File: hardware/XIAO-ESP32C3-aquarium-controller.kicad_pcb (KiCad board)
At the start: 2 copper layers, 70 x 100 mm, 43 parts, among them J1 Conn_01x02, J2 Conn_01x07, J3 Conn_01x06, J4 Conn_01x03, J5 Conn_01x03, K1 SANYOU_SRD_Form_C, K2 SANYOU_SRD_Form_C, K3 SANYOU_SRD_Form_C, Q1 AO3400A, Q2 AO3400A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

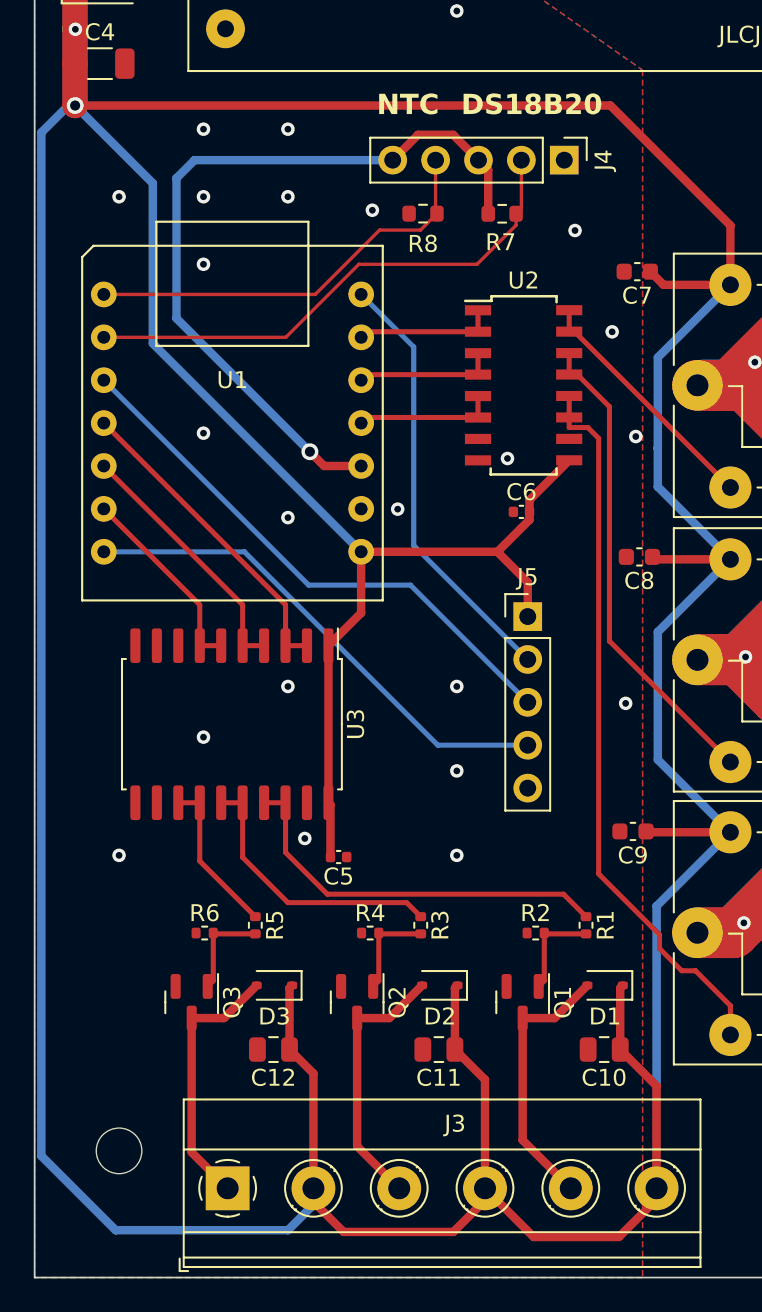
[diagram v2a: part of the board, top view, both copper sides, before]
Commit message: add + pad for 5V
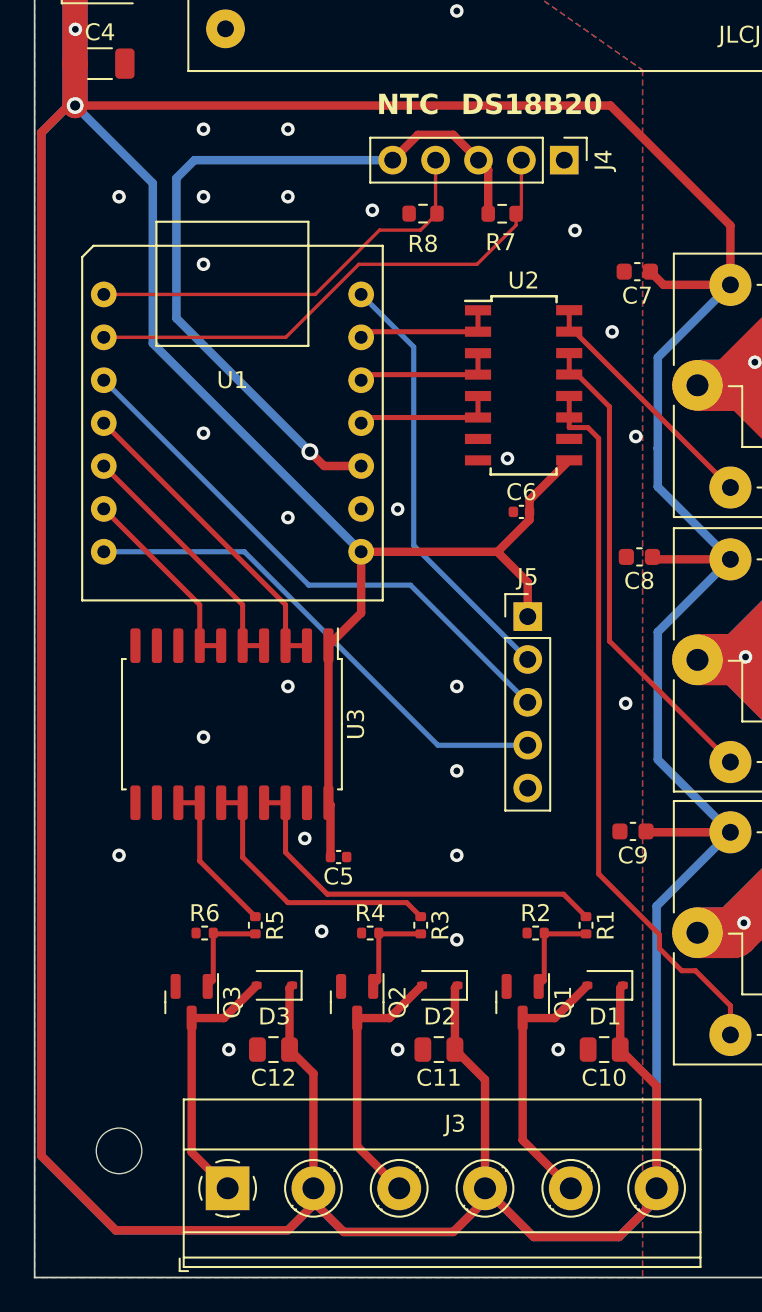
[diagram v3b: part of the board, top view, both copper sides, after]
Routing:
- net +5V: track 404.1 -> 513.0 mm
- net GND: vias 24 -> 29
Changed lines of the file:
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@@
     (effects (font (size 1 1) (thickness 0.15)) (justify left bottom))
   )
-  (segment (start 48.11 122.51) (end 49.9 124.3) (width 0.5) (layer "F.Cu") (net 1))
+  (segment locked (start 48.11 122.51) (end 49.9 124.3) (width 0.5) (layer "F.Cu") (net 1))
   (segment (start 33.994 55.118) (end 33.994 57.594) (width 1.5) (layer "F.Cu") (net 1))
   (segment (start 68.43 121.717) (end 68.43 115.653) (width 0.5) (layer "F.Cu") (net 1))
-  (segment (start 56.4 124.3) (end 58.27 122.43) (width 0.5) (layer "F.Cu") (net 1))
+  (segment locked (start 56.4 124.3) (end 58.27 122.43) (width 0.5) (layer "F.Cu") (net 1))
   (segment (start 68.843 68.218) (end 68.062 67.437) (width 0.5) (layer "F.Cu") (net 1))
   (segment (start 46.695 109.855) (end 46.85 109.7) (width 0.5) (layer "F.Cu") (net 1))
-  (segment (start 66.2 124.6) (end 68.43 122.37) (width 0.5) (layer "F.Cu") (net 1))
+  (segment locked (start 66.2 124.6) (end 68.43 122.37) (width 0.5) (layer "F.Cu") (net 1))
   (segment (start 72.802 64.702) (end 72.802 68.218) (width 0.5) (layer "F.Cu") (net 1))
   (segment (start 60.909 82.128229) (end 60.909 81.661) (width 0.5) (layer "F.Cu") (net 1))
   (segment (start 67.858 100.634) (end 67.808 100.584) (width 0.5) (layer "F.Cu") (net 1))
   (segment (start 50.93575 84.0245) (end 50.93575 87.64725) (width 0.5) (layer "F.Cu") (net 1))
-  (segment (start 49.9 124.3) (end 56.4 124.3) (width 0.5) (layer "F.Cu") (net 1))
+  (segment (start 36.4 124.2) (end 46.6 124.2) (width 0.5) (layer "F.Cu") (net 1))
+  (segment locked (start 49.9 124.3) (end 56.4 124.3) (width 0.5) (layer "F.Cu") (net 1))
   (segment (start 72.802 100.634) (end 67.858 100.634) (width 0.5) (layer "F.Cu") (net 1))
   (segment (start 60.8 85.8245) (end 59 84.0245) (width 0.5) (layer "F.Cu") (net 1))
@@
   (segment (start 60.8 87.86) (end 60.8 85.8245) (width 0.5) (layer "F.Cu") (net 1))
   (segment (start 33.994 50.1705) (end 33.994 55.118) (width 1.5) (layer "F.Cu") (net 1))
+  (segment (start 32 59.2) (end 32 119.8) (width 0.5) (layer "F.Cu") (net 1))
   (segment (start 59.012729 84.0245) (end 60.909 82.128229) (width 0.5) (layer "F.Cu") (net 1))
   (segment (start 34 57.6) (end 65.7 57.6) (width 0.5) (layer "F.Cu") (net 1))
   (segment (start 66.277 109.855) (end 66.432 109.7) (width 0.5) (layer "F.Cu") (net 1))
   (segment (start 34.481621 41.618379) (end 34.481621 42.418) (width 1.5) (layer "F.Cu") (net 1))
-  (segment (start 68.43 122.37) (end 68.43 121.717) (width 0.5) (layer "F.Cu") (net 1))
-  (segment (start 58.27 122.43) (end 58.27 121.717) (width 0.5) (layer "F.Cu") (net 1))
+  (segment (start 33.6 57.6) (end 32 59.2) (width 0.5) (layer "F.Cu") (net 1))
+  (segment locked (start 68.43 122.37) (end 68.43 121.717) (width 0.5) (layer "F.Cu") (net 1))
+  (segment locked (start 58.27 122.43) (end 58.27 121.717) (width 0.5) (layer "F.Cu") (net 1))
+  (segment (start 46.6 124.2) (end 48.11 122.69) (width 0.5) (layer "F.Cu") (net 1))
   (segment (start 34.481621 42.418) (end 34.1265 42.773121) (width 1.5) (layer "F.Cu") (net 1))
   (segment (start 50.93575 87.64725) (end 48.999 89.584) (width 0.5) (layer "F.Cu") (net 1))
+  (segment (start 48.11 122.69) (end 48.11 121.717) (width 0.5) (layer "F.Cu") (net 1))
   (segment (start 66.277 113.5) (end 66.277 109.855) (width 0.5) (layer "F.Cu") (net 1))
+  (segment (start 34 57.6) (end 33.6 57.6) (width 0.5) (layer "F.Cu") (net 1))
+  (segment (start 32 119.8) (end 36.4 124.2) (width 0.5) (layer "F.Cu") (net 1))
   (segment (start 34.1265 50.038) (end 33.994 50.1705) (width 1.5) (layer "F.Cu") (net 1))
   (segment (start 68.43 115.653) (end 66.277 113.5) (width 0.5) (layer "F.Cu") (net 1))
-  (segment (start 58.27 121.717) (end 61.153 124.6) (width 0.5) (layer "F.Cu") (net 1))
+  (segment locked (start 58.27 121.717) (end 61.153 124.6) (width 0.5) (layer "F.Cu") (net 1))
   (segment (start 48.999 89.584) (end 48.999 98.884) (width 0.5) (layer "F.Cu") (net 1))
   (segment (start 33.994 57.594) (end 34 57.6) (width 1.5) (layer "F.Cu") (net 1))
@@
   (segment (start 49.12 99.005) (end 48.999 98.884) (width 0.5) (layer "F.Cu") (net 1))
   (segment (start 50.93575 84.0245) (end 59 84.0245) (width 0.5) (layer "F.Cu") (net 1))
-  (segment (start 48.11 121.717) (end 48.11 122.51) (width 0.5) (layer "F.Cu") (net 1))
+  (segment locked (start 48.11 121.717) (end 48.11 122.51) (width 0.5) (layer "F.Cu") (net 1))
   (segment (start 59 84.0245) (end 59.012729 84.0245) (width 0.5) (layer "F.Cu") (net 1))
   (segment (start 42.9035 33.1965) (end 34.481621 41.618379) (width 1.5) (layer "F.Cu") (net 1))
   (segment (start 58.27 115.2818) (end 56.4882 113.5) (width 0.5) (layer "F.Cu") (net 1))
   (segment (start 60.909 81.661) (end 60.909 80.955) (width 0.5) (layer "F.Cu") (net 1))
-  (segment (start 61.153 124.6) (end 66.2 124.6) (width 0.5) (layer "F.Cu") (net 1))
+  (segment locked (start 61.153 124.6) (end 66.2 124.6) (width 0.5) (layer "F.Cu") (net 1))
   (segment (start 58.27 121.717) (end 58.27 115.2818) (width 0.5) (layer "F.Cu") (net 1))
   (segment (start 60.909 80.955) (end 63.256 78.608) (width 0.5) (layer "F.Cu") (net 1))
@@
   (segment (start 33.6 57.6) (end 32 59.2) (width 0.5) (layer "B.Cu") (net 1))
   (segment (start 72.802 84.474) (end 68.502 88.774) (width 0.5) (layer "B.Cu") (net 1))
+  (segment (start 56.4 124.3) (end 58.27 122.43) (width 0.5) (layer "B.Cu") (net 1))
+  (segment (start 66.1985 124.6) (end 68.4285 122.37) (width 0.5) (layer "B.Cu") (net 1))
   (segment (start 46.6 124.2) (end 48.11 122.69) (width 0.5) (layer "B.Cu") (net 1))
+  (segment (start 49.9 124.3) (end 56.4 124.3) (width 0.5) (layer "B.Cu") (net 1))
   (segment (start 32 119.8) (end 36.4 124.2) (width 0.5) (layer "B.Cu") (net 1))
   (segment (start 68.5 77.9) (end 68.5 80.172) (width 0.5) (layer "B.Cu") (net 1))
   (segment (start 34.481621 42.418) (end 34 42.899621) (width 1.5) (layer "B.Cu") (net 1))
   (segment (start 72.802 100.634) (end 68.43 105.006) (width 0.5) (layer "B.Cu") (net 1))
+  (segment (start 58.27 122.43) (end 58.27 121.717) (width 0.5) (layer "B.Cu") (net 1))
   (segment (start 68.502 96.334) (end 72.802 100.634) (width 0.5) (layer "B.Cu") (net 1))
   (segment (start 34 53.073) (end 34.013 53.086) (width 1.5) (layer "B.Cu") (net 1))
+  (segment (start 48.11 122.51) (end 49.9 124.3) (width 0.5) (layer "B.Cu") (net 1))
+  (segment (start 58.2685 121.717) (end 61.1515 124.6) (width 0.5) (layer "B.Cu") (net 1))
   (segment (start 42.910939 33.18906) (end 34.48906 41.610939) (width 1.5) (layer "B.Cu") (net 1))
   (segment (start 68.502 77.898) (end 68.5 77.9) (width 0.5) (layer "B.Cu") (net 1))
   (segment (start 68.5 80.172) (end 72.802 84.474) (width 0.5) (layer "B.Cu") (net 1))
   (segment (start 34 57.6) (end 38.6 62.2) (width 0.5) (layer "B.Cu") (net 1))
+  (segment (start 61.1515 124.6) (end 66.1985 124.6) (width 0.5) (layer "B.Cu") (net 1))
   (segment (start 38.6 71.68875) (end 50.93575 84.0245) (width 0.5) (layer "B.Cu") (net 1))
+  (segment (start 68.4285 122.37) (end 68.4285 121.717) (width 0.5) (layer "B.Cu") (net 1))
   (segment (start 68.43 105.006) (end 68.43 121.717) (width 0.5) (layer "B.Cu") (net 1))
+  (segment (start 48.11 121.717) (end 48.11 122.51) (width 0.5) (layer "B.Cu") (net 1))
   (segment (start 34 57.6) (end 33.6 57.6) (width 0.5) (layer "B.Cu") (net 1))
   (segment (start 32 59.2) (end 32 119.8) (width 0.5) (layer "B.Cu") (net 1))
@@
   (segment (start 36.4 124.2) (end 46.6 124.2) (width 0.5) (layer "B.Cu") (net 1))
   (segment (start 72.802 68.218) (end 68.502 72.518) (width 0.5) (layer "B.Cu") (net 1))
+  (via (at 48.6 106.5) (size 0.8) (drill 0.4) (layers "F.Cu" "B.Cu") (free) (net 2))
   (via (at 66.6 93) (size 0.8) (drill 0.4) (layers "F.Cu" "B.Cu") (free) (net 2))
+  (via (at 56.6 107) (size 0.8) (drill 0.4) (layers "F.Cu" "B.Cu") (free) (net 2))
   (via (at 41.6 95) (size 0.8) (drill 0.4) (layers "F.Cu" "B.Cu") (free) (net 2))
   (via (at 53.1 81.5) (size 0.8) (drill 0.4) (layers "F.Cu" "B.Cu") (free) (net 2))
@@
   (via (at 51.6 63.8) (size 0.8) (drill 0.4) (layers "F.Cu" "B.Cu") (free) (net 2))
   (via (at 59.6 78.5) (size 0.8) (drill 0.4) (layers "F.Cu" "B.Cu") (free) (net 2))
+  (via (at 53.1 113.5) (size 0.8) (drill 0.4) (layers "F.Cu" "B.Cu") (free) (net 2))
   (via (at 56.6 52) (size 0.8) (drill 0.4) (layers "F.Cu" "B.Cu") (free) (net 2))
   (via (at 63.6 65) (size 0.8) (drill 0.4) (layers "F.Cu" "B.Cu") (free) (net 2))
   (via (at 46.6 47) (size 0.8) (drill 0.4) (layers "F.Cu" "B.Cu") (free) (net 2))
   (via (at 36.6 102) (size 0.8) (drill 0.4) (layers "F.Cu" "B.Cu") (free) (net 2))
+  (via (at 62.6 113.5) (size 0.8) (drill 0.4) (layers "F.Cu" "B.Cu") (free) (net 2))
   (via (at 65.8 71) (size 0.8) (drill 0.4) (layers "F.Cu" "B.Cu") (free) (net 2))
+  (via (at 43.1 113.5) (size 0.8) (drill 0.4) (layers "F.Cu" "B.Cu") (free) (net 2))
   (via (at 41.6 77) (size 0.8) (drill 0.4) (layers "F.Cu" "B.Cu") (free) (net 2))
   (via (at 46.6 82) (size 0.8) (drill 0.4) (layers "F.Cu" "B.Cu") (free) (net 2))

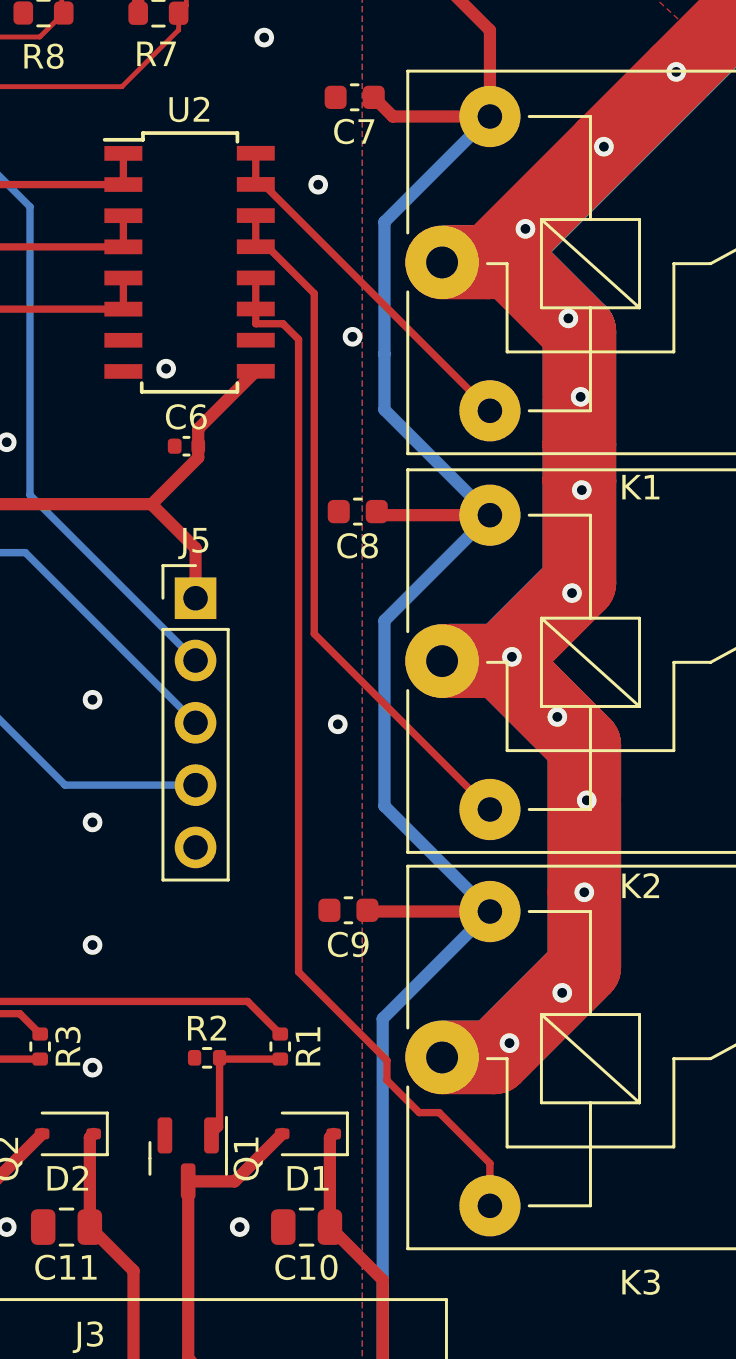
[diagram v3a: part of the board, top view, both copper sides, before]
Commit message: ticker pads for relay
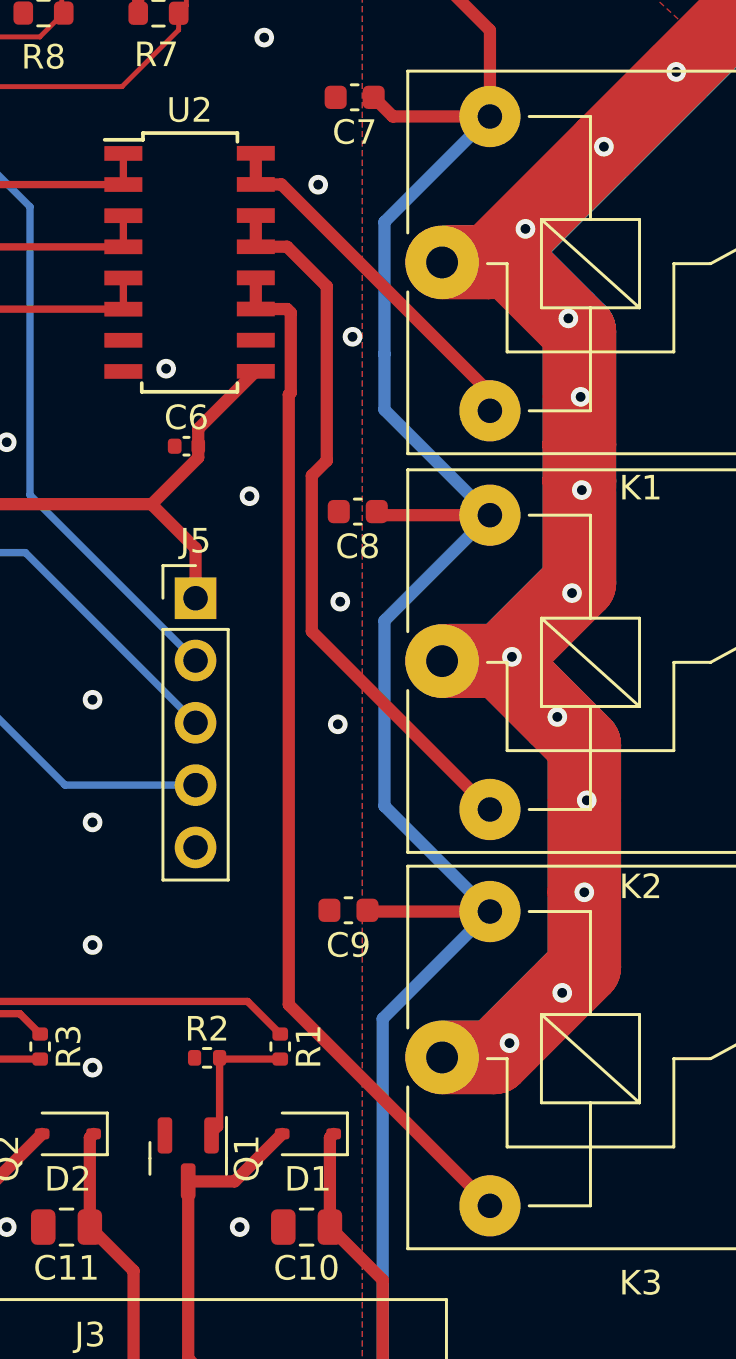
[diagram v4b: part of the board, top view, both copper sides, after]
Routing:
- net /rel2: track 28.4 -> 29.4 mm
- net GND: vias 29 -> 31
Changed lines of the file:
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@@
   (via (at 41.6 67) (size 0.8) (drill 0.4) (layers "F.Cu" "B.Cu") (free) (net 2))
   (via (at 67.2 77.2) (size 0.8) (drill 0.4) (layers "F.Cu" "B.Cu") (free) (net 2))
+  (via (at 63 83.7) (size 0.8) (drill 0.4) (layers "F.Cu" "B.Cu") (free) (net 2))
   (via (at 56.6 92) (size 0.8) (drill 0.4) (layers "F.Cu" "B.Cu") (free) (net 2))
   (via (at 41.6 59) (size 0.8) (drill 0.4) (layers "F.Cu" "B.Cu") (free) (net 2))
@@
   (via (at 62.6 113.5) (size 0.8) (drill 0.4) (layers "F.Cu" "B.Cu") (free) (net 2))
   (via (at 65.8 71) (size 0.8) (drill 0.4) (layers "F.Cu" "B.Cu") (free) (net 2))
+  (via (at 66.7 88) (size 0.8) (drill 0.4) (layers "F.Cu" "B.Cu") (free) (net 2))
   (via (at 43.1 113.5) (size 0.8) (drill 0.4) (layers "F.Cu" "B.Cu") (free) (net 2))
   (via (at 41.6 77) (size 0.8) (drill 0.4) (layers "F.Cu" "B.Cu") (free) (net 2))
@@
   (segment (start 54.45 64.975) (end 55.425 64) (width 0.2) (layer "F.Cu") (net 17))
   (segment (start 48.2155 68.7845) (end 52.025 64.975) (width 0.2) (layer "F.Cu") (net 17))
-  (segment (start 63.256 70.988) (end 63.256 69.718) (width 0.3) (layer "F.Cu") (net 18))
-  (segment (start 63.572 70.988) (end 72.802 80.218) (width 0.3) (layer "F.Cu") (net 18))
-  (segment (start 63.256 70.988) (end 63.572 70.988) (width 0.3) (layer "F.Cu") (net 18))
-  (segment (start 63.731 73.528) (end 65.639 75.436) (width 0.3) (layer "F.Cu") (net 19))
-  (segment (start 65.639 89.311) (end 72.802 96.474) (width 0.3) (layer "F.Cu") (net 19))
-  (segment (start 63.256 73.528) (end 63.256 72.258) (width 0.3) (layer "F.Cu") (net 19))
-  (segment (start 63.256 73.528) (end 63.731 73.528) (width 0.3) (layer "F.Cu") (net 19))
-  (segment (start 65.639 75.436) (end 65.639 89.311) (width 0.3) (layer "F.Cu") (net 19))
-  (segment (start 72.802 110.902) (end 72.802 112.634) (width 0.3) (layer "F.Cu") (net 20))
-  (segment (start 70.734 108.834) (end 72.802 110.902) (width 0.3) (layer "F.Cu") (net 20))
-  (segment (start 69.920019 108.834) (end 70.734 108.834) (width 0.3) (layer "F.Cu") (net 20))
-  (segment (start 63.256 76.668) (end 64.361 76.668) (width 0.3) (layer "F.Cu") (net 20))
-  (segment (start 64.361 76.668) (end 65 77.307) (width 0.3) (layer "F.Cu") (net 20))
-  (segment (start 63.256 76.068) (end 63.256 74.798) (width 0.3) (layer "F.Cu") (net 20))
-  (segment (start 68.602 106.702) (end 68.602 107.515981) (width 0.3) (layer "F.Cu") (net 20))
-  (segment (start 65 103.1) (end 68.602 106.702) (width 0.3) (layer "F.Cu") (net 20))
-  (segment (start 68.602 107.515981) (end 69.920019 108.834) (width 0.3) (layer "F.Cu") (net 20))
-  (segment (start 63.256 76.068) (end 63.256 76.668) (width 0.3) (layer "F.Cu") (net 20))
-  (segment (start 65 77.307) (end 65 103.1) (width 0.3) (layer "F.Cu") (net 20))
+  (segment (start 63.256 69.718) (end 63.256 70.988) (width 0.5) (layer "F.Cu") (net 18))
+  (segment (start 72.802 79.486925) (end 72.802 80.218) (width 0.5) (layer "F.Cu") (net 18))
+  (segment (start 63.256 70.988) (end 64.303075 70.988) (width 0.5) (layer "F.Cu") (net 18))
+  (segment (start 64.303075 70.988) (end 72.802 79.486925) (width 0.5) (layer "F.Cu") (net 18))
+  (segment (start 66.15 75.147) (end 66.15 82.25) (width 0.5) (layer "F.Cu") (net 19))
+  (segment (start 64.531 73.528) (end 66.15 75.147) (width 0.5) (layer "F.Cu") (net 19))
+  (segment (start 66.15 82.25) (end 65.539 82.861) (width 0.5) (layer "F.Cu") (net 19))
+  (segment (start 65.539 89.211) (end 72.802 96.474) (width 0.5) (layer "F.Cu") (net 19))
+  (segment (start 63.256 73.528) (end 64.531 73.528) (width 0.5) (layer "F.Cu") (net 19))
+  (segment (start 65.539 82.861) (end 65.539 89.211) (width 0.5) (layer "F.Cu") (net 19))
+  (segment (start 63.256 72.258) (end 63.256 73.528) (width 0.5) (layer "F.Cu") (net 19))
+  (segment (start 63.256 76.068) (end 64.531 76.068) (width 0.5) (layer "F.Cu") (net 20))
+  (segment (start 64.6 79.558) (end 64.6 104.432) (width 0.5) (layer "F.Cu") (net 20))
+  (segment (start 63.256 74.798) (end 63.256 76.068) (width 0.5) (layer "F.Cu") (net 20))
+  (segment (start 64.531 76.068) (end 64.681 76.218) (width 0.5) (layer "F.Cu") (net 20))
+  (segment (start 64.681 76.218) (end 64.681 79.477) (width 0.5) (layer "F.Cu") (net 20))
+  (segment (start 64.6 104.432) (end 72.802 112.634) (width 0.5) (layer "F.Cu") (net 20))
+  (segment (start 64.681 79.477) (end 64.6 79.558) (width 0.5) (layer "F.Cu") (net 20))
   (segment (start 61.78 109.4325) (end 61.45 109.7625) (width 0.3) (layer "F.Cu") (net 21))
   (segment (start 64.252 106.65) (end 61.83 106.65) (width 0.3) (layer "F.Cu") (net 21))

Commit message: fixed 10K resistor for NTC Thermistor
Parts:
- R8: value 4K7 -> 10K
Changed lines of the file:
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@@
         (effects (font (size 1 1) (thickness 0.15)))
     )
-    (fp_text value "4K7" (at 0 1.43) (layer "F.Fab")
+    (fp_text value "10K" (at 0 1.43) (layer "F.Fab")
         (effects (font (size 1 1) (thickness 0.15)))
     )
